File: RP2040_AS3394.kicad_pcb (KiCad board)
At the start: 4 copper layers, 51.8 x 68.3 mm, 130 parts, among them J1 Conn_01x03, J2 TYPE-C-31-M-12, J3 Conn_01x02, J4 Conn_01x08, J5 Conn_01x03, U1 RP2040, U2 NCP1117-3.3_SOT223, U3 W25Q128JVS, U4 LM324, U5 AS3394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

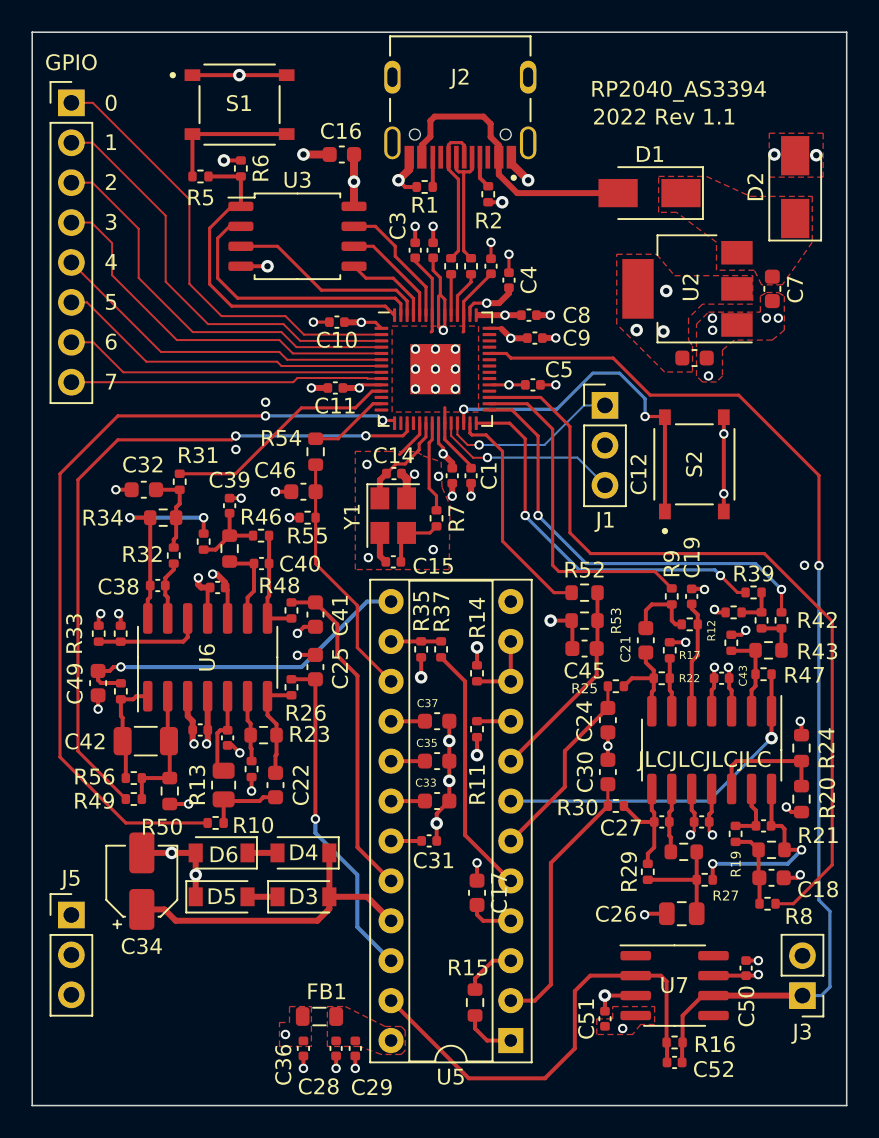
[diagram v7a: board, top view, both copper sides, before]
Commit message: added separate LDO for 3394, removed amp, designed psu board and made project for carrier board
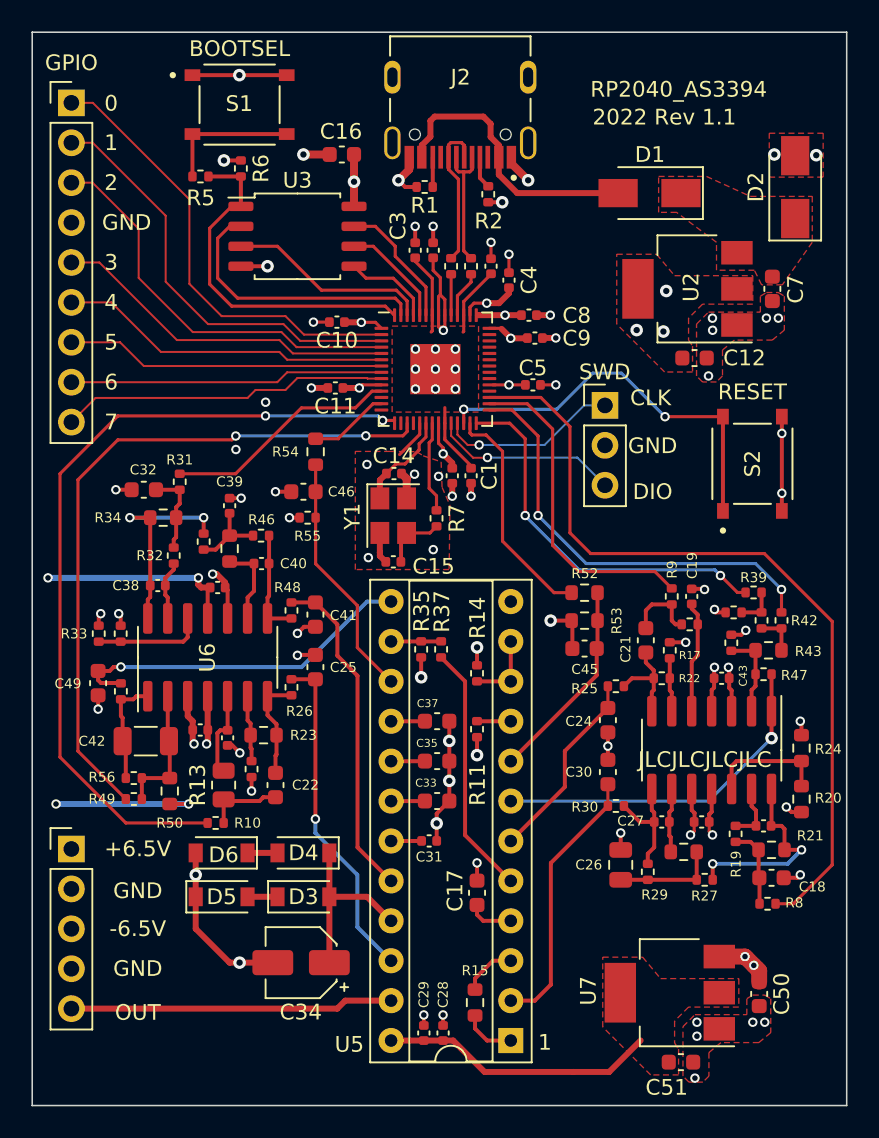
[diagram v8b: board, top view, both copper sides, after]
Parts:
- removed C36: 1u, Capacitor_SMD:C_0402_1005Metric
- removed C52: 47p, Capacitor_SMD:C_0402_1005Metric
- removed FB1: 120R, Inductor_SMD:L_0805_2012Metric
- removed J5: Conn_01x03, Connector_PinHeader_2.54mm:PinHeader_1x03_P2.54mm_Vertical
- removed R16: 7.5k, Resistor_SMD:R_0402_1005Metric
- C17: value 1n5 -> 2n
- C28: value 10n -> 0.1u
- C50, C51: value 0.1u -> 10u; footprint Capacitor_SMD:C_0402_1005Metric -> Capacitor_SMD:C_0603_1608Metric
- J3: value Conn_01x02 -> Conn_01x05; footprint Connector_PinHeader_2.54mm:PinHeader_1x02_P2.54mm_Vertical -> Connector_PinHeader_2.54mm:PinHeader_1x05_P2.54mm_Vertical
- J4: value Conn_01x08 -> Conn_01x09; footprint Connector_PinHeader_2.54mm:PinHeader_1x08_P2.54mm_Vertical -> Connector_PinHeader_2.54mm:PinHeader_1x09_P2.54mm_Vertical
- U7: value TL071 -> NCP1117-5.0_SOT223; footprint Package_SO:SOIC-8_3.9x4.9mm_P1.27mm -> Package_TO_SOT_SMD:SOT-223-3_TabPin2
- moved J3 47.5 mm to (111.5, 135.5), turned to 0 degrees
- moved C34 11.4 mm to (126.1, 142.7), turned to 180 degrees
- moved C28 6.88 mm to (135.1, 147.2), turned to 90 degrees
- moved C51 5.57 mm to (150.3, 149.1), turned to 0 degrees
- moved C26 4.98 mm to (146.4, 136.5), turned to 90 degrees
- moved C29 4.47 mm to (133.9, 147.2), turned to 90 degrees
- moved S2 3.69 mm to (154.8, 111.0)
- moved C50 1.84 mm to (155.2, 144.7), turned to -90 degrees
- moved U7 0.54 mm to (149.6, 144.7), turned to 180 degrees
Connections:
- C28 pad 1: Net-(C28-Pad1) -> +5V
- C29 pad 1: Net-(C28-Pad1) -> +5V
- C51 pad 1: VEE -> +5V
- J3 pad 1: /AMP_OUT -> VCC
- J4 pad 4: Net-(J4-Pad4) -> GND
- J4 pad 5: Net-(J4-Pad5) -> Net-(U1-Pad5)
- J4 pad 6: Net-(J4-Pad6) -> Net-(U1-Pad6)
- J4 pad 7: Net-(J4-Pad7) -> Net-(U1-Pad7)
- J4 pad 8: Net-(J4-Pad8) -> Net-(U1-Pad8)
- U1 pad 38: /AMP_OUT -> unconnected-(U1-Pad38)
- U1 pad 5: Net-(J4-Pad4) -> Net-(U1-Pad5)
- U1 pad 6: Net-(J4-Pad5) -> Net-(U1-Pad6)
- U1 pad 7: Net-(J4-Pad6) -> Net-(U1-Pad7)
- U1 pad 8: Net-(J4-Pad7) -> Net-(U1-Pad8)
- U1 pad 9: Net-(J4-Pad8) -> Net-(U1-Pad9)
- U5 pad 24: Net-(C28-Pad1) -> +5V
- U7 pad 1: unconnected-(U7-Pad1) -> GND
- U7 pad 2: /AS3394_PWM/Out -> +5V
- U7 pad 3: GND -> VCC
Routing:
- net /AMP_OUT: track 70.2 -> 0.00 mm, vias 1 -> 0
- net Net-(J4-Pad4): track 24.4 -> 0.00 mm
- net Net-(J4-Pad5): track 22.3 -> 0.00 mm
- net Net-(U1-Pad5): track 0.00 -> 22.1 mm
- net Net-(J4-Pad6): track 21.4 -> 0.00 mm
- net Net-(U1-Pad6): track 0.00 -> 21.2 mm
- net Net-(U1-Pad9): track 0.00 -> 20.9 mm
- net Net-(J4-Pad7): track 20.5 -> 0.00 mm
- net Net-(U1-Pad7): track 0.00 -> 20.4 mm
- net Net-(U1-Pad8): track 0.00 -> 20.0 mm
- net Net-(J4-Pad8): track 19.9 -> 0.00 mm
- net +5V: track 0.00 -> 17.5 mm
- net Net-(C34-Pad1): track 20.7 -> 11.2 mm
- net /AS3394_PWM/Out: track 29.7 -> 20.6 mm
- net /RUN: track 22.5 -> 25.5 mm
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- added copper zone on F.Cu, net +5V
- removed copper zone on F.Cu, net Net-(C28-Pad1)
- removed copper zone on F.Cu, net VEE
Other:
- board text added: "+6.5V"
- board text added: "-6.5V"
- board text added: "BOOTSEL"
- board text added: "CLK"
- board text added: "DIO"
- board text added: "GND"
- board text added: "OUT"
- board text added: "RESET"
- board text added: "SWD"
